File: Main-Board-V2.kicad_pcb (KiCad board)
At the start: 2 copper layers, 31 parts, among them IC1 REG1117-5, J1 770669-5, J2 BCS-114-L-S-PE-BE, J3 BCS-114-L-S-PE-BE, J4 776280-1, J5 776280-1, J6 DT15-2P, K1 J107F1AS123VDC.36, K2 J107F1AS123VDC.36, K3 J107F1AS123VDC.36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

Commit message: Idk what but it is better than before
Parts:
- removed J1: 770669-5, 770669-5:TE_770669-5
- removed J2, J3: BCS-114-L-S-PE-BE, BCS:SAMTEC_BCS-114-L-S-PE-BE
- removed J6: DT15-2P, DT15-2P:TE_DT15-2P
- removed K3: J107F1AS123VDC.36, PRE29-5V-S-450-1A-E:RELAY_PRE29-5V-S-450-1A-E
- removed Q3: 2N2222A, 2N2222A:TO92254P470H750-3
- added J7: 776163-5, 776163-5:TE_776163-5, F.Cu at (50.5, 92.5)
- added U10: OPA325IDBVR, OPA325IDBVR:SOT95P280X145-5N, F.Cu at (113.0, 76.2)
- added U11: Teensy4.0, Custom:Teensy40_Raised, F.Cu at (125.2, 117.9)
- added U9: VOM618A-3T, VOM618A-3T:SOIC254P695X242-4N, F.Cu at (154.9, 78.7)
- moved J5 129.3 mm to (244.2, 134.6), turned to 90 degrees
- moved J4 122.4 mm to (245.5, 76.2), turned to 90 degrees
- moved U4 103.0 mm to (72.4, 122.8)
- moved U5 103.0 mm to (72.4, 129.3)
- moved U6 103.0 mm to (72.4, 135.9)
- moved U7 103.0 mm to (72.4, 142.4)
- moved U8 102.8 mm to (72.7, 150.2)
- moved IC1 102.8 mm to (105.4, 156.2)
- moved C1 100.4 mm to (105.4, 161.3), turned to 180 degrees
- moved C2 92.0 mm to (102.9, 149.9), turned to 180 degrees
- moved U2 69.4 mm to (227.8, 47.6)
- moved U1 68.9 mm to (108.0, 69.8)
- moved U3 60.6 mm to (116.8, 85.1)
- moved C4 53.9 mm to (213.1, 35.5)
- moved C5 53.9 mm to (212.6, 37.8)
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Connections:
- J4 pad 5: unconnected-(J4-Pad5) -> Net-(J4-Pad5)
- J4 pad 6: unconnected-(J4-Pad6) -> Net-(J4-Pad6)
- J4 pad 7: unconnected-(J4-Pad7) -> Net-(J4-Pad7)
- J4 pad 8: unconnected-(J4-Pad8) -> Net-(J4-Pad8)
- J5 pad 5: unconnected-(J5-Pad5) -> Net-(J4-Pad5)
- J5 pad 6: unconnected-(J5-Pad6) -> Net-(J4-Pad6)
- J5 pad 7: unconnected-(J5-Pad7) -> Net-(J4-Pad7)
- J5 pad 8: unconnected-(J5-Pad8) -> Net-(J4-Pad8)
- K1 pad 3: /Relays/RightIndicator -> /Relays/BattOut
- K1 pad 4: +12V -> /Relays/BattIn
- K2 pad 3: /Relays/LeftIndicator -> /Relays/Radio+
- K2 pad 4: +12V -> /Relays/Radio-
- Q1 pad 2: /Relays/RightTurnSignal -> /BattEnable
- Q2 pad 2: /Relays/BattRelay -> Net-(Q2-Pad2)
- Q2 pad 3: Net-(K3-Pad1) -> Net-(K2-Pad1)
- U1 pad 4: /Throttle- -> GND
- U3 pad 4: /DigitalInputs/BrakeIO -> /Pedal/ErrorIO
- U4 pad 4: /DigitalInputs/Dio3 -> /Button3
- U5 pad 4: /DigitalInputs/Dio4 -> /Button4
- U6 pad 4: /DigitalInputs/Dio0 -> /Button0
- U7 pad 4: /DigitalInputs/Dio1 -> /Button1
- U8 pad 4: /DigitalInputs/Dio2 -> /Button2
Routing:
- net /Can/CaNH: track 0.00 -> 62.3 mm
- net Net-(J4-Pad8): track 0.00 -> 60.6 mm
- net Net-(J4-Pad6): track 0.00 -> 60.6 mm
- net Net-(J4-Pad7): track 0.00 -> 60.5 mm
- net /Can/CaNL: track 0.00 -> 60.3 mm
- net Net-(J4-Pad5): track 0.00 -> 60.0 mm
- net +5V: track 0.00 -> 26.4 mm
- net +12V: track 0.00 -> 3.61 mm

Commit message: There is something different. Will fix soon, previous save is better
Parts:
- removed the J5 at (244.2, 134.6)
- removed the J7 at (50.5, 92.5)
- added J5: 776280-1, 776280-1:TE_776280-1, F.Cu at (76.8, 93.7)
- added J5: 776280-1, 776280-1:TE_776280-1, F.Cu at (76.2, 50.8)
- added J7: 776163-5, 776163-5:TE_776163-5, F.Cu at (203.2, 50.0)
- added J7: 776163-5, 776163-5:TE_776163-5, F.Cu at (301.0, 50.0)
- moved U8 179.0 mm to (244.0, 98.2)
- moved U4 179.0 mm to (244.0, 72.0)
- moved U5 179.0 mm to (244.0, 78.6)
- moved U6 179.0 mm to (244.0, 85.1)
- moved U7 179.0 mm to (244.0, 91.7)
- moved U1 177.6 mm to (285.6, 71.0)
- moved U3 176.6 mm to (293.0, 72.0)
- moved U10 172.5 mm to (285.6, 75.4)
- moved U2 132.1 mm to (97.8, 71.1), turned to 90 degrees
- moved D1 114.8 mm to (109.2, 81.3), turned to 90 degrees
- moved L1 111.4 mm to (113.0, 67.4), turned to 90 degrees
- moved J4 111.3 mm to (137.2, 50.8), turned to 180 degrees
- moved D2 104.9 mm to (118.1, 81.3), turned to 90 degrees
- moved L2 104.5 mm to (118.1, 64.8), turned to 90 degrees
- moved U9 102.0 mm to (255.6, 95.5)
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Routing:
- net /Can/CaNH: track 62.3 -> 0.00 mm
- net Net-(J4-Pad8): track 60.6 -> 0.00 mm
- net Net-(J4-Pad6): track 60.6 -> 0.00 mm
- net Net-(J4-Pad7): track 60.5 -> 0.00 mm
- net /Can/CaNL: track 60.3 -> 0.00 mm
- net Net-(J4-Pad5): track 60.0 -> 0.00 mm
- net +5V: track 26.4 -> 0.00 mm
- net +12V: track 3.61 -> 0.00 mm

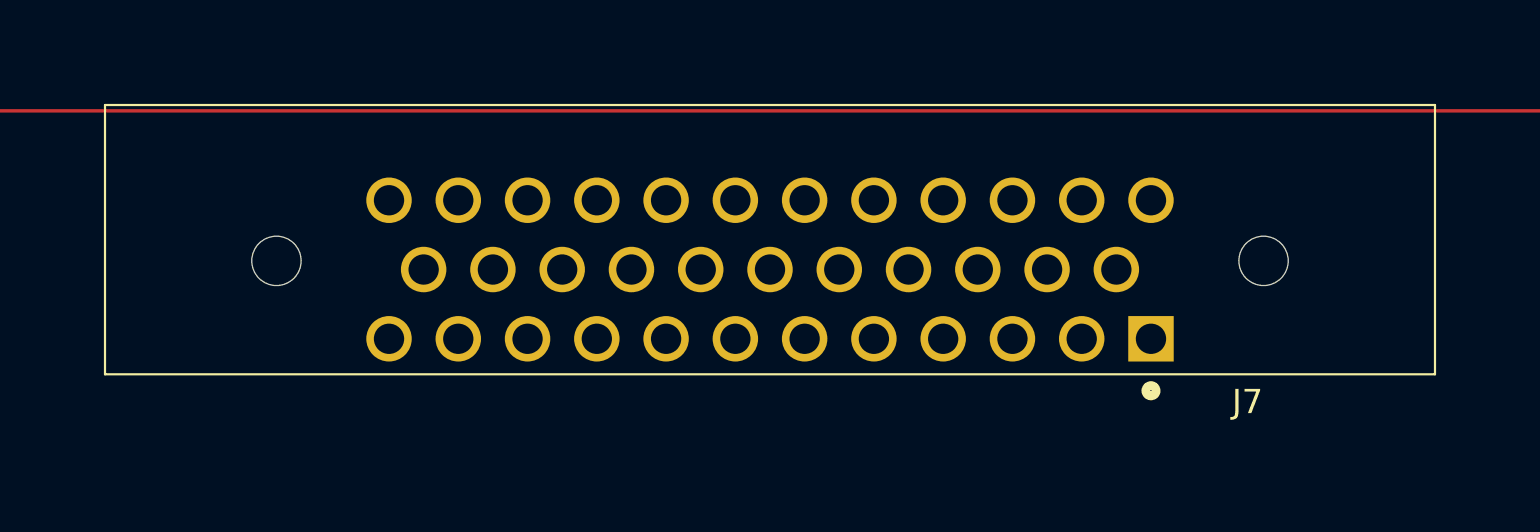
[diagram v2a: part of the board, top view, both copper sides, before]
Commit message: made connector match drawing
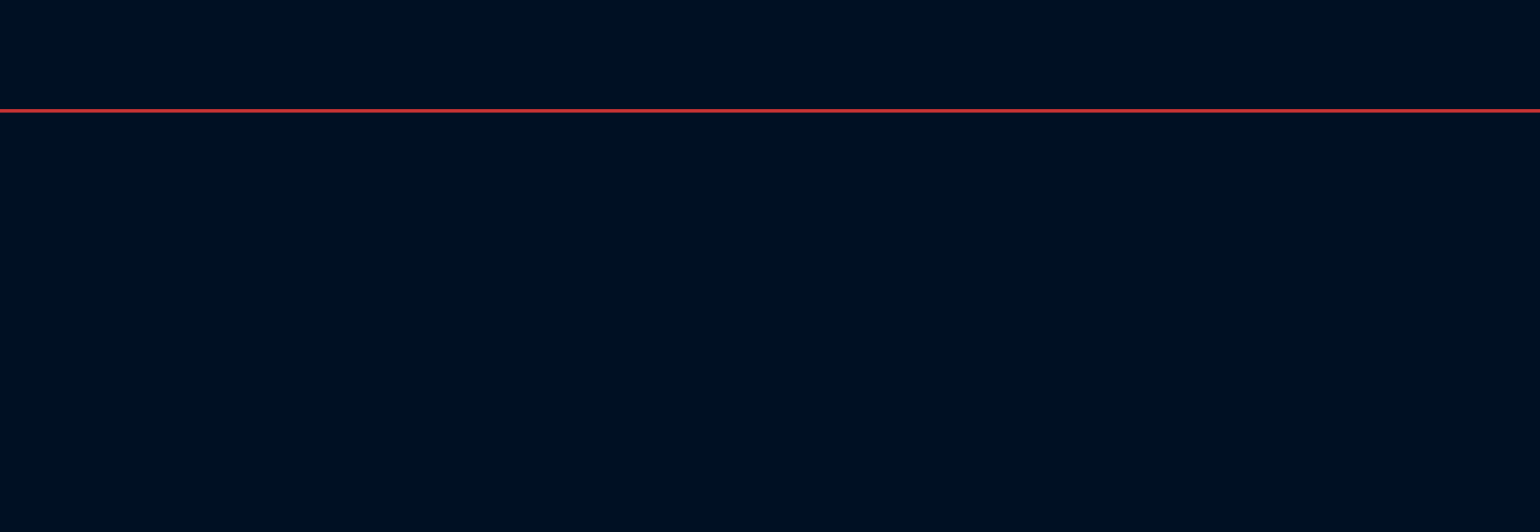
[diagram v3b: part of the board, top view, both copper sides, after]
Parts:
- removed the J7 at (301.0, 50.0)

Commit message: placed most components
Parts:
- removed C1: 10U, Cap10U:CAPC2012X145N
- removed J5 (x2): 776280-1, 776280-1:TE_776280-1
- removed J7: 776163-5, 776163-5:TE_776163-5
- removed U2: ADM3057EBRWZ, ADM3057EBRWZ:SOIC127P1032X265-20N
- added C3: 10U, Cap10U:CAPC2012X145N, F.Cu at (226.4, 167.1)
- added J2: 776280-1, 776280-1:TE_776280-1, F.Cu at (164.4, 80.3)
- added J3: 776280-1, 776280-1:TE_776280-1, F.Cu at (164.3, 121.2)
- added K3: J107F1AS123VDC.36, PRE29-5V-S-450-1A-E:RELAY_PRE29-5V-S-450-1A-E, F.Cu at (390.3, 90.3)
- added Q3: 2N2222A, 2N2222A:TO92254P470H750-3, F.Cu at (390.3, 103.0)
- added R1: R_US, Resistor_SMD:R_0805_2012Metric, F.Cu at (333.1, 110.8)
- added R10: 10K, Resistor_SMD:R_0805_2012Metric, F.Cu at (267.1, 99.8)
- added R11: 10K, Resistor_SMD:R_0805_2012Metric, F.Cu at (291.3, 99.8)
- added R12: 10K, Resistor_SMD:R_0805_2012Metric, F.Cu at (299.5, 84.6)
- added R13: 10K, Resistor_SMD:R_0805_2012Metric, F.Cu at (283.6, 83.9)
- added R14: 10K, Resistor_SMD:R_0805_2012Metric, F.Cu at (276.0, 83.9)
- added R15: 10K, Resistor_SMD:R_0805_2012Metric, F.Cu at (298.9, 99.2)
- added R16: 10K, Resistor_SMD:R_0805_2012Metric, F.Cu at (282.4, 100.5)
- added R17: 10K, Resistor_SMD:R_0805_2012Metric, F.Cu at (274.7, 99.8)
- added R18: 10K, Resistor_SMD:R_0805_2012Metric, F.Cu at (260.1, 83.9)
- added R19: 10K, Resistor_SMD:R_0805_2012Metric, F.Cu at (258.9, 99.8)
- added R2: R_US, Resistor_SMD:R_0805_2012Metric, F.Cu at (328.6, 111.4)
- added R20: R_US, Resistor_SMD:R_0805_2012Metric, F.Cu at (343.4, 111.6)
- added R21: R_US, Resistor_SMD:R_0805_2012Metric, F.Cu at (368.1, 108.0)
- added R22: R_US, Resistor_SMD:R_0805_2012Metric, F.Cu at (343.4, 114.6)
- added R23: R_US, Resistor_SMD:R_0805_2012Metric, F.Cu at (364.7, 108.0)
- added R24: R_US, Resistor_SMD:R_0805_2012Metric, F.Cu at (347.7, 115.0)
- added R25: R_US, Resistor_SMD:R_0805_2012Metric, F.Cu at (360.4, 106.7)
- added R26: R_US, Resistor_SMD:R_0805_2012Metric, F.Cu at (347.5, 107.2)
- added R27: R_US, Resistor_SMD:R_0805_2012Metric, F.Cu at (364.7, 112.1)
- added R28: R_US, Resistor_SMD:R_0805_2012Metric, F.Cu at (343.2, 107.2)
- added R29: R_US, Resistor_SMD:R_0805_2012Metric, F.Cu at (368.0, 112.2)
- added R3: R_US, Resistor_SMD:R_0805_2012Metric, F.Cu at (328.6, 107.6)
- added R30: 10K, Resistor_SMD:R_0805_2012Metric, F.Cu at (405.6, 77.6)
- added R31: 10K, Resistor_SMD:R_0805_2012Metric, F.Cu at (389.7, 78.2)
- added R4: R_US, Resistor_SMD:R_0805_2012Metric, F.Cu at (328.6, 115.2)
- added R5: R_US, Resistor_SMD:R_0805_2012Metric, F.Cu at (322.9, 115.2)
- added R8: 10K, Resistor_SMD:R_0805_2012Metric, F.Cu at (267.8, 83.9)
- added R9: 10K, Resistor_SMD:R_0805_2012Metric, F.Cu at (291.9, 83.9)
- added REF**: Teensy 4.0, teensy.pretty-master:Teensy40_SMT, F.Cu at (224.5, 98.6)
- J4: value 776280-1 -> 1-776231-4; footprint 776280-1:TE_776280-1 -> 1-776231-4:TE_1-776231-4
- R6, R7: footprint Resistor_SMD:R_0603_1608Metric -> Resistor_SMD:R_0805_2012Metric
- U11: value Teensy4.0 -> OPA325IDBVR; footprint Custom:Teensy40_Raised -> OPA325IDBVR:SOT95P280X145-5N
- U3: value VOM618A-3T -> ADM3057EBRWZ; footprint VOM618A-3T:SOIC254P695X242-4N -> ADM3057EBRWZ:SOIC127P1032X265-20N
- moved J4 209.4 mm to (343.3, 87.6), turned to 0 degrees
- moved U11 190.8 mm to (360.3, 110.9), turned to 180 degrees
- moved IC1 181.4 mm to (230.1, 158.2)
- moved C2 174.0 mm to (226.4, 164.1)
- moved K1 158.7 mm to (419.5, 90.3), turned to 90 degrees
- moved Q1 147.4 mm to (420.0, 103.1)
- moved K2 143.4 mm to (404.9, 90.3), turned to 90 degrees
- moved Q2 131.5 mm to (404.9, 103.0)
- moved L2 130.1 mm to (212.6, 154.2), turned to 0 degrees
- moved L1 130.0 mm to (212.6, 150.9), turned to 0 degrees
- moved C4 127.5 mm to (209.1, 159.0), turned to 0 degrees
- moved C5 124.3 mm to (208.6, 161.3), turned to 0 degrees
- moved R6 121.0 mm to (204.9, 159.2), turned to 0 degrees
- moved D1 119.9 mm to (206.4, 151.4), turned to 0 degrees
- moved R7 116.0 mm to (204.9, 162.1), turned to 0 degrees
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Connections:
- net /BattEnable renamed /Relays/BattRelay
- C2 pad 1: GND -> GNDp
- C2 pad 2: +5V -> +12V
- J4 pad 1: +12V -> unconnected-(J4-Pad1)
- J4 pad 2: GNDp -> unconnected-(J4-Pad2)
- J4 pad 3: /Can/CaNH -> /DigitalInputs/Button1
- J4 pad 4: /Can/CaNL -> /DigitalInputs/Button2
- J4 pad 5: Net-(J4-Pad5) -> /DigitalInputs/Button3
- J4 pad 6: Net-(J4-Pad6) -> /Radio-
- J4 pad 7: Net-(J4-Pad7) -> /Radio-
- J4 pad 8: Net-(J4-Pad8) -> /Pedal/Error
- K2 pad 3: /Relays/Radio+ -> Net-(K2-Pad3)
- K2 pad 4: /Relays/Radio- -> +12V
- Q2 pad 2: Net-(Q2-Pad2) -> /Relays/LeftSigIn
- U3 pad 1: Net-(R8-Pad2) (its old number) -> GND
- U3 pad 2: GNDp -> GND
- U3 pad 3: GND -> +5V
- U3 pad 4: /Pedal/ErrorIO -> +3.3V
- U4 pad 4: /Button3 -> /DigitalInputs/Dio3
- U5 pad 4: /Button4 -> /DigitalInputs/Dio4
- U6 pad 4: /Button0 -> /DigitalInputs/Dio5
- U7 pad 4: /Button1 -> /DigitalInputs/Dio1
- U8 pad 4: /Button2 -> /DigitalInputs/Dio2
- U9 pad 2: GNDp -> GND
- U9 pad 3: Net-(Q2-Pad2) -> GND
- U9 pad 4: /RadioButton -> /Pedal/ErrorIO
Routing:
- net /Pedal/Error: track 0.00 -> 97.0 mm
- net /Relays/BattOut: track 0.00 -> 76.7 mm
- net /DigitalInputs/Button3: track 0.00 -> 73.7 mm
- net /DigitalInputs/Button2: track 0.00 -> 60.4 mm
- net /Relays/BattIn: track 0.00 -> 56.9 mm
- net /DigitalInputs/Button1: track 0.00 -> 47.8 mm
- net /Relays/RightSignal: track 0.00 -> 47.6 mm
- net /DigitalInputs/Button4: track 0.00 -> 46.1 mm
- net /DigitalInputs/Button5: track 0.00 -> 42.7 mm
- net GND: track 0.00 -> 41.1 mm
- net /Relays/LeftSignal: track 0.00 -> 35.1 mm
- net /Pedal/Brake+: track 0.00 -> 34.4 mm, vias 0 -> 1
- net /Pedal/Throttle+: track 0.00 -> 34.2 mm, vias 0 -> 1
- net /Encoder: track 0.00 -> 31.2 mm, vias 0 -> 1
- net Net-(U1-OUT): track 0.00 -> 8.80 mm
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- added copper zone on B.Cu, net GND
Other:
- copper layers 2 -> 4

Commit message: replaced CAN chip, power planes
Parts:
- removed D1, D2: SMAJ36CA, SMAJ36CA:SMASERIES-M
- removed L1, L2: 100BR, RN73C2B100RBTDF:RESC3015X65N
- removed R6: R8, Resistor_SMD:R_0805_2012Metric
- removed R7: 10R, Resistor_SMD:R_0805_2012Metric
- added C8: 0.1U, GRT155C80J105KE01J:CAPC1005X55N, F.Cu at (149.3, 108.7)
- added C9: 0.1U, GRT155C80J105KE01J:CAPC1005X55N, F.Cu at (155.4, 101.0)
- added U12: MCP2562-E_SN, MCP2562-E_SN:SOIC127P600X175-8N, F.Cu at (155.2, 106.1)
- C4: value 4U7 -> 0.1U; footprint GRM188R61E475KE11D:CAPC1608X95N -> GRT155C80J105KE01J:CAPC1005X55N
- C5: value 1U -> 0.1U
- U3: value ADM3057EBRWZ -> MCP2562-E_SN; footprint ADM3057EBRWZ:SOIC127P1032X265-20N -> MCP2562-E_SN:SOIC127P600X175-8N
- moved C3 95.4 mm to (191.5, 78.4), turned to -90 degrees
- moved IC1 85.3 mm to (197.7, 79.4)
- moved C2 84.7 mm to (194.5, 85.6), turned to 90 degrees
- moved C4 65.4 mm to (179.4, 100.7)
- moved C5 63.7 mm to (173.6, 108.1), turned to -90 degrees
- moved U3 47.5 mm to (179.6, 105.8), turned to -90 degrees
- moved R19 1.39 mm to (260.2, 100.1), turned to 0 degrees
- moved R17 1.27 mm to (276.0, 100.1), turned to 0 degrees
- moved R11 1.08 mm to (292.2, 99.4), turned to 0 degrees
- moved R16 0.70 mm to (282.7, 99.9)
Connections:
- net /Can/CaNH renamed Net-(J2-Pad3)
- net Net-(J2-Pad6) renamed /Can/CaNL1
- net Net-(J2-Pad7) renamed /Can/CaNH1
- C2 pad 1: GNDp -> GND
- C4 pad 1: /Can/VCC50CANx -> +5V
- C4 pad 2: /Can/GNDCanx -> GND
- C5 pad 1: /Can/VCC50CAN -> GND
- C5 pad 2: /Can/GNDCan -> +3.3V
- J2 pad 2: GNDp -> GND
- J2 pad 4: /Can/CaNL -> /Can/CaNL0
- J2 pad 5: Net-(J2-Pad5) -> /Can/CaNH0
- J3 pad 2: GNDp -> GND
- J3 pad 4: /Can/CaNL -> /Can/CaNL0
- J3 pad 5: Net-(J2-Pad5) -> /Can/CaNH0
- U3 pad 1: GND -> /Can/CanTx0
- U3 pad 4: +3.3V -> /Can/CanRx0
- U3 pad 5: /Can/CanRx -> +3.3V
- U3 pad 6: GND -> /Can/CaNL0
- U3 pad 7: /Can/CanTx -> /Can/CaNH0
- U4 pad 2: GNDp -> GND
- U5 pad 2: GNDp -> GND
- U6 pad 2: GNDp -> GND
- U7 pad 2: GNDp -> GND
- U8 pad 2: GNDp -> GND
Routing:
- net +5V: track 0.00 -> 311.4 mm, vias 0 -> 4
- net +12V: track 0.00 -> 290.3 mm
- net +3.3V: track 0.00 -> 193.2 mm, vias 0 -> 6
- net /Relays/BattRelay: track 0.00 -> 130.0 mm
- net /Relays/LeftSigIn: track 0.00 -> 111.1 mm
- net /Can/CaNH1: track 0.00 -> 105.9 mm
- net /Relays/RightSigIn: track 0.00 -> 92.2 mm
- net /Can/CaNL1: track 0.00 -> 81.3 mm
- net /Can/CaNH0: track 0.00 -> 76.8 mm
- net Net-(J2-Pad8): track 0.00 -> 73.5 mm
- net /Can/CaNL0: track 0.00 -> 72.4 mm
- net /Pedal/ThrottleIO: track 0.00 -> 68.5 mm, vias 0 -> 1
- net GND: track 41.1 -> 107.9 mm, vias 0 -> 6
- net /Can_RX1: track 0.00 -> 54.8 mm
- net /Pedal/BrakeIO: track 0.00 -> 47.8 mm, vias 0 -> 1
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- added copper zone on In2.Cu, net +12V
- added copper zone on In2.Cu, net +3.3V

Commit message: Finished routing
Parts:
- removed REF**: Teensy 4.0, teensy.pretty-master:Teensy40_SMT
- added U2: Teensy4.0, teensy.pretty-master:Teensy40_SMT, F.Cu at (137.8, 95.7)
- moved C2 90.5 mm to (104.6, 75.8)
- moved C3 90.5 mm to (101.6, 68.6)
- moved C5 90.5 mm to (83.7, 98.3)
- moved IC1 90.5 mm to (107.8, 69.6)
- moved J3 90.5 mm to (74.4, 111.4)
- moved K1 90.5 mm to (329.6, 80.5)
- moved K3 90.5 mm to (300.4, 80.5)
- moved Q3 90.5 mm to (300.4, 93.2)
- moved R1 90.5 mm to (243.2, 101.0)
- moved R10 90.5 mm to (177.2, 90.0)
- moved R12 90.5 mm to (209.6, 74.8)
- moved R13 90.5 mm to (193.7, 74.2)
- moved R14 90.5 mm to (186.1, 74.2)
- moved R15 90.5 mm to (208.9, 89.4)
- moved R18 90.5 mm to (170.2, 74.2)
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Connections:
- net /DigitalInputs/Dio1 renamed /Dio1
- net /DigitalInputs/Dio2 renamed /Dio2
- net /DigitalInputs/Dio3 renamed /Dio3
- net /DigitalInputs/Dio4 renamed /Dio4
- net /DigitalInputs/Dio5 renamed /Dio5
- net /Pedal/ErrorIO renamed /ErrorIO
- J4 pad 1: unconnected-(J4-Pad1) -> /USART_RX
- J4 pad 13: unconnected-(J4-Pad13) -> /USART_TX
- Q1 pad 2: /Relays/BattRelay -> /BattRelay
- Q2 pad 2: /Relays/LeftSigIn -> /LeftSignalIO
- Q3 pad 2: /Relays/RightSigIn -> /RightSignalIO
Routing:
- net /BattRelay: track 0.00 -> 198.3 mm
- net /LeftSignalIO: track 0.00 -> 182.9 mm
- net /RightSignalIO: track 0.00 -> 167.9 mm
- net /Relays/BattRelay: track 130.0 -> 0.00 mm
- net /USART_TX: track 0.00 -> 119.4 mm
- net /USART_RX: track 0.00 -> 116.8 mm
- net /Relays/LeftSigIn: track 111.1 -> 0.00 mm
- net /Relays/RightSigIn: track 92.2 -> 0.00 mm
- net /Pedal/ThrottleIO: track 68.5 -> 158.3 mm
- net /EncoderIO: track 19.1 -> 106.8 mm
- net /Pedal/BrakeIO: track 47.8 -> 135.3 mm
- net /Dio5: track 4.56 -> 91.6 mm
- net /Can_TX1: track 46.9 -> 128.5 mm, vias 0 -> 1
- net /Dio4: track 4.83 -> 81.2 mm
- net /Dio1: track 5.09 -> 71.7 mm
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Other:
- board outline added: 350 x 60 mm

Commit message: I've been a busy boy
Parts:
- added G***: LOGO, LOGO, B.Cu at (77.3, 91.0)
- added G***: LOGO, LOGO, B.Cu at (173.5, 86.0)
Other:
- outline, holes or cut-outs redrawn
- board text added: "1"
- board text added: "10"
- board text added: "11"
- board text added: "12"
- board text added: "13"
- board text added: "14"
- board text added: "15"
- board text added: "16"
- board text added: "17"
- board text added: "18"
- board text added: "19"
- board text added: "2"
- board text added: "20"
- board text added: "21"
- board text added: "22"
- board text added: "23"
- board text added: "24"
- board text added: "25"
- board text added: "26"
- board text added: "27"
- board text added: "28"
- board text added: "29"
- board text added: "3"
- board text added: "30"
- board text added: "31"
- board text added: "32"
- board text added: "33"
- board text added: "34"
- board text added: "4"
- board text added: "5"
- board text added: "6"
- board text added: "7"
- board text added: "8"
- board text added: "9"

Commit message: Added silkscreen logo
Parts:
- removed the G*** at (77.3, 91.0)
- moved G*** 26.5 mm to (199.5, 91.0)
